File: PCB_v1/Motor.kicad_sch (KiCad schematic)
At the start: 18 parts, among them J10 B4B-XH-A, U6 DRV8834PWP

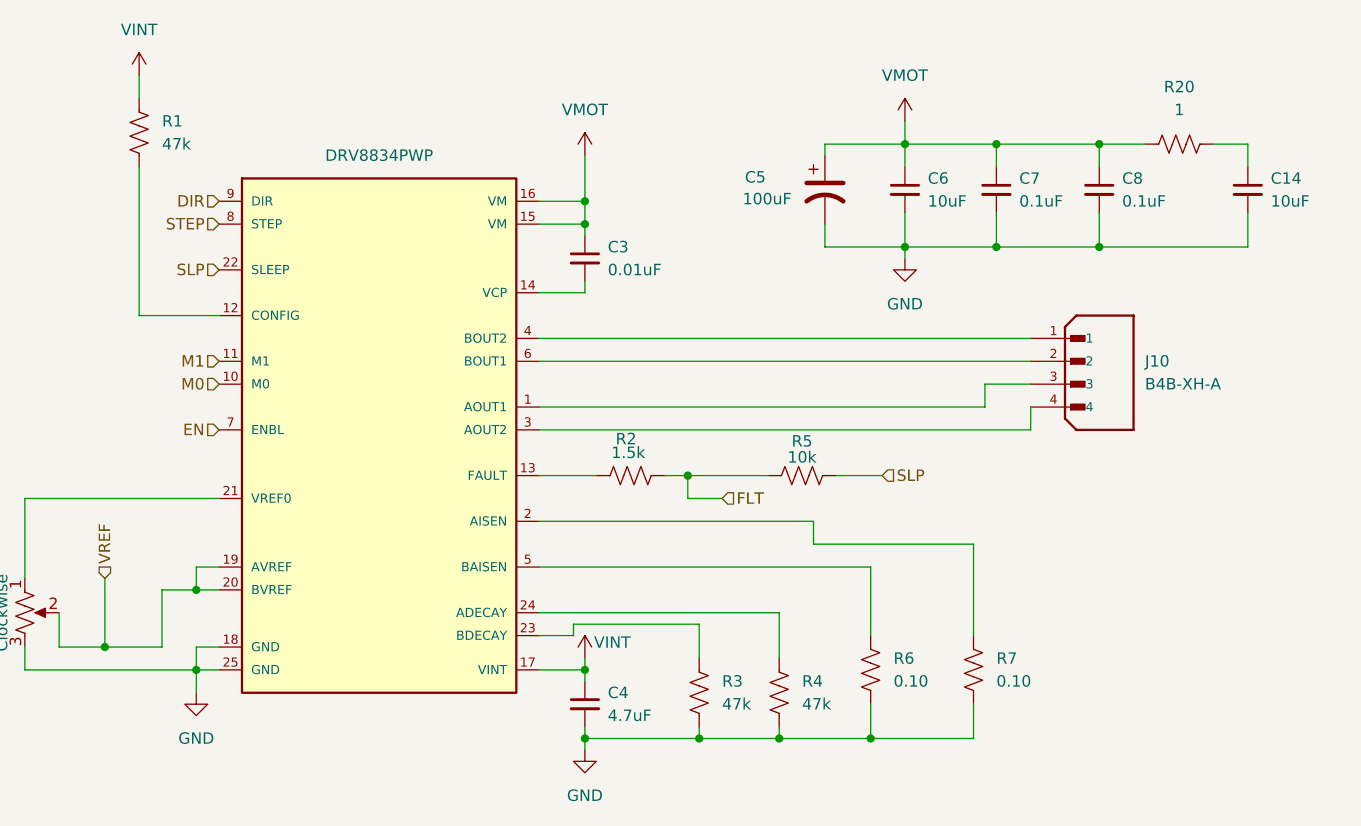
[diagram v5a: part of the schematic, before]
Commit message: Update before adding AGND for the power delivery
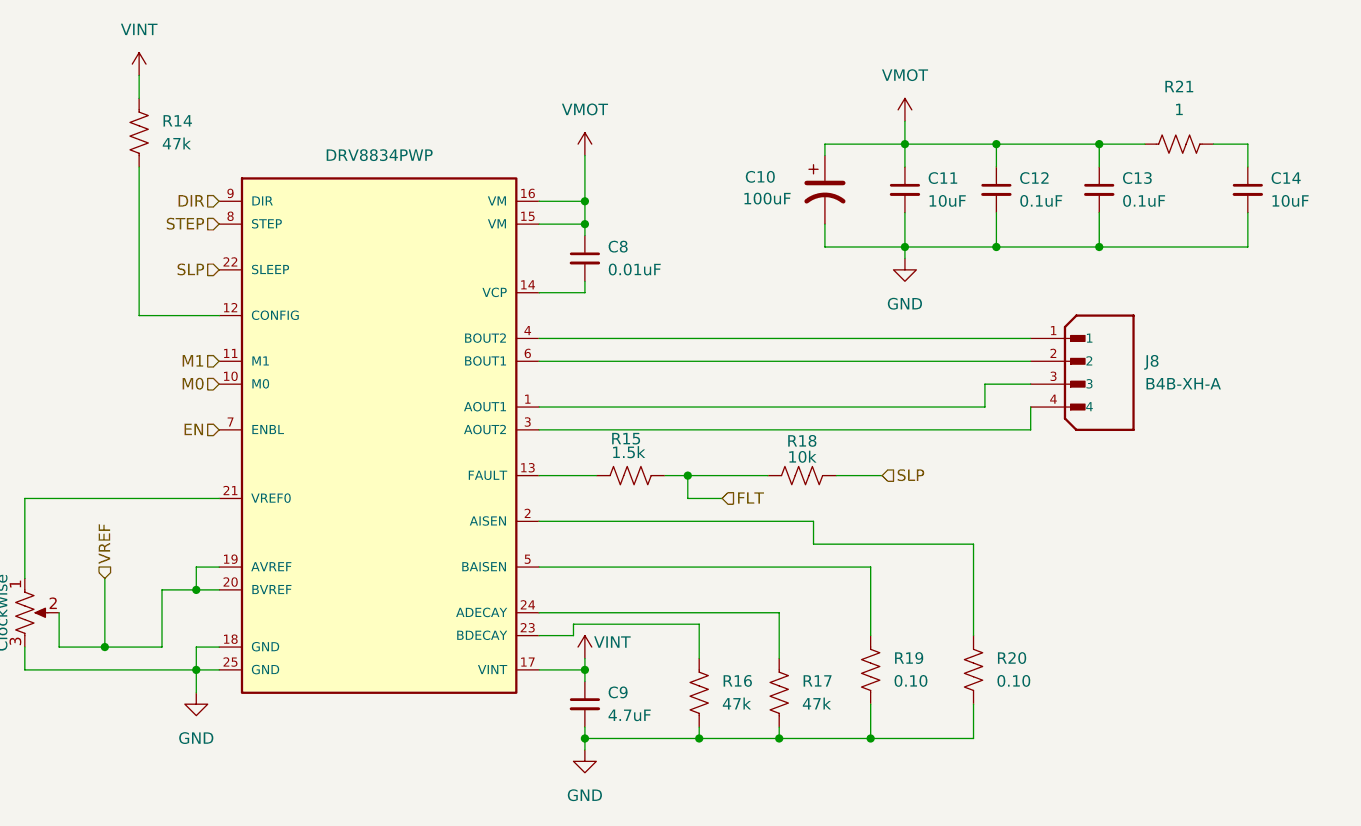
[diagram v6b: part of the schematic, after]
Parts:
- renumbered C5 to C10, C6 to C11, C7 to C12, C8 to C13, C3 to C8, C4 to C9, J10 to J8, R1 to R14, R2 to R15, R3 to R16, R4 to R17, R5 to R18, R6 to R19, R7 to R20, R20 to R21, U6 to U4
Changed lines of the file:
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@@
 		(dnp no)
 		(fields_autoplaced yes)
-		(property "Reference" "#PWR073"
+		(property "Reference" "#PWR074"
 			(at 256.54 96.52 0)
 			(effects
@@
 			(project "tuner time"
 				(path "/353cef6a-fb6e-40d9-89f8-eb54b7aa5118/2d8cfae4-f7d1-4a7d-b5cb-7588b4c1e8a5"
-					(reference "#PWR073")
+					(reference "#PWR074")
 					(unit 1)
 				)
@@
 		(dnp no)
 		(fields_autoplaced yes)
-		(property "Reference" "R1"
+		(property "Reference" "R14"
 			(at 81.28 57.1499 0)
 			(effects
@@
 			(project "tuner time"
 				(path "/353cef6a-fb6e-40d9-89f8-eb54b7aa5118/2d8cfae4-f7d1-4a7d-b5cb-7588b4c1e8a5"
-					(reference "R1")
+					(reference "R14")
 					(unit 1)
 				)
@@
 		(dnp no)
 		(fields_autoplaced yes)
-		(property "Reference" "#PWR070"
+		(property "Reference" "#PWR073"
 			(at 245.11 93.98 0)
 			(effects
@@
 			(project "tuner time"
 				(path "/353cef6a-fb6e-40d9-89f8-eb54b7aa5118/2d8cfae4-f7d1-4a7d-b5cb-7588b4c1e8a5"
-					(reference "#PWR070")
+					(reference "#PWR073")
 					(unit 1)
 				)
@@
 		(dnp no)
 		(fields_autoplaced yes)
-		(property "Reference" "R3"
+		(property "Reference" "R16"
 			(at 143.51 119.3799 0)
 			(effects
@@
 			(project "tuner time"
 				(path "/353cef6a-fb6e-40d9-89f8-eb54b7aa5118/2d8cfae4-f7d1-4a7d-b5cb-7588b4c1e8a5"
-					(reference "R3")
+					(reference "R16")
 					(unit 1)
 				)
@@
 		(dnp no)
 		(fields_autoplaced yes)
-		(property "Reference" "R20"
+		(property "Reference" "R21"
 			(at 194.31 53.34 90)
 			(effects
@@
 			(project "tuner time"
 				(path "/353cef6a-fb6e-40d9-89f8-eb54b7aa5118/2d8cfae4-f7d1-4a7d-b5cb-7588b4c1e8a5"
-					(reference "R20")
+					(reference "R21")
 					(unit 1)
 				)
@@
 		(dnp no)
 		(fields_autoplaced yes)
-		(property "Reference" "C3"
+		(property "Reference" "C8"
 			(at 130.81 71.1262 0)
 			(effects
@@
 			(project "tuner time"
 				(path "/353cef6a-fb6e-40d9-89f8-eb54b7aa5118/2d8cfae4-f7d1-4a7d-b5cb-7588b4c1e8a5"
-					(reference "C3")
+					(reference "C8")
 					(unit 1)
 				)
@@
 		(dnp no)
 		(fields_autoplaced yes)
-		(property "Reference" "#PWR067"
+		(property "Reference" "#PWR070"
 			(at 163.83 60.96 0)
 			(effects
@@
 			(project "tuner time"
 				(path "/353cef6a-fb6e-40d9-89f8-eb54b7aa5118/2d8cfae4-f7d1-4a7d-b5cb-7588b4c1e8a5"
-					(reference "#PWR067")
+					(reference "#PWR070")
 					(unit 1)
 				)
@@
 		(dnp no)
 		(fields_autoplaced yes)
-		(property "Reference" "#PWR064"
+		(property "Reference" "#PWR067"
 			(at 128.27 64.77 0)
 			(effects
@@
 			(project "tuner time"
 				(path "/353cef6a-fb6e-40d9-89f8-eb54b7aa5118/2d8cfae4-f7d1-4a7d-b5cb-7588b4c1e8a5"
-					(reference "#PWR064")
+					(reference "#PWR067")
 					(unit 1)
 				)
@@
 		(dnp no)
 		(fields_autoplaced yes)
-		(property "Reference" "#PWR066"
+		(property "Reference" "#PWR069"
 			(at 128.27 133.35 0)
 			(effects
@@
 			(project "tuner time"
 				(path "/353cef6a-fb6e-40d9-89f8-eb54b7aa5118/2d8cfae4-f7d1-4a7d-b5cb-7588b4c1e8a5"
-					(reference "#PWR066")
+					(reference "#PWR069")
 					(unit 1)
 				)
@@
 		(dnp no)
 		(fields_autoplaced yes)
-		(property "Reference" "#PWR063"
+		(property "Reference" "#PWR065"
 			(at 78.74 55.88 0)
 			(effects
@@
 			(project "tuner time"
 				(path "/353cef6a-fb6e-40d9-89f8-eb54b7aa5118/2d8cfae4-f7d1-4a7d-b5cb-7588b4c1e8a5"
-					(reference "#PWR063")
+					(reference "#PWR065")
 					(unit 1)
 				)
@@
 		(dnp no)
 		(fields_autoplaced yes)
-		(property "Reference" "#PWR062"
+		(property "Reference" "#PWR066"
 			(at 85.09 127 0)
 			(effects
@@
 			(project "tuner time"
 				(path "/353cef6a-fb6e-40d9-89f8-eb54b7aa5118/2d8cfae4-f7d1-4a7d-b5cb-7588b4c1e8a5"
-					(reference "#PWR062")
+					(reference "#PWR066")
 					(unit 1)
 				)
@@
 		(dnp no)
 		(fields_autoplaced yes)
-		(property "Reference" "R4"
+		(property "Reference" "R17"
 			(at 152.4 119.3799 0)
 			(effects
@@
 			(project "tuner time"
 				(path "/353cef6a-fb6e-40d9-89f8-eb54b7aa5118/2d8cfae4-f7d1-4a7d-b5cb-7588b4c1e8a5"
-					(reference "R4")
+					(reference "R17")
 					(unit 1)
 				)
@@
 		(dnp no)
 		(fields_autoplaced yes)
-		(property "Reference" "C7"
+		(property "Reference" "C12"
 			(at 176.53 63.5062 0)
 			(effects
@@
 			(project "tuner time"
 				(path "/353cef6a-fb6e-40d9-89f8-eb54b7aa5118/2d8cfae4-f7d1-4a7d-b5cb-7588b4c1e8a5"
-					(reference "C7")
+					(reference "C12")
 					(unit 1)
 				)
@@
 		(dnp no)
 		(fields_autoplaced yes)
-		(property "Reference" "U6"
+		(property "Reference" "U4"
 			(at 105.41 58.42 0)
 			(effects
@@
 			(project "tuner time"
 				(path "/353cef6a-fb6e-40d9-89f8-eb54b7aa5118/2d8cfae4-f7d1-4a7d-b5cb-7588b4c1e8a5"
-					(reference "U6")
+					(reference "U4")
 					(unit 1)
 				)
@@
 		(dnp no)
 		(fields_autoplaced yes)
-		(property "Reference" "#PWR069"
+		(property "Reference" "#PWR072"
 			(at 238.76 93.98 0)
 			(effects
@@
 			(project "tuner time"
 				(path "/353cef6a-fb6e-40d9-89f8-eb54b7aa5118/2d8cfae4-f7d1-4a7d-b5cb-7588b4c1e8a5"
-					(reference "#PWR069")
+					(reference "#PWR072")
 					(unit 1)
 				)
@@
 		(dnp no)
 		(fields_autoplaced yes)
-		(property "Reference" "C8"
+		(property "Reference" "C13"
 			(at 187.96 63.5062 0)
 			(effects
@@
 			(project "tuner time"
 				(path "/353cef6a-fb6e-40d9-89f8-eb54b7aa5118/2d8cfae4-f7d1-4a7d-b5cb-7588b4c1e8a5"
-					(reference "C8")
+					(reference "C13")
 					(unit 1)
 				)
@@
 		(dnp no)
 		(fields_autoplaced yes)
-		(property "Reference" "#PWR068"
+		(property "Reference" "#PWR071"
 			(at 163.83 78.74 0)
 			(effects
@@
 			(project "tuner time"
 				(path "/353cef6a-fb6e-40d9-89f8-eb54b7aa5118/2d8cfae4-f7d1-4a7d-b5cb-7588b4c1e8a5"
-					(reference "#PWR068")
+					(reference "#PWR071")
 					(unit 1)
 				)
@@
 		(dnp no)
 		(fields_autoplaced yes)
-		(property "Reference" "C6"
+		(property "Reference" "C11"
 			(at 166.37 63.5062 0)
 			(effects
@@
 			(project "tuner time"
 				(path "/353cef6a-fb6e-40d9-89f8-eb54b7aa5118/2d8cfae4-f7d1-4a7d-b5cb-7588b4c1e8a5"
-					(reference "C6")
+					(reference "C11")
 					(unit 1)
 				)
@@
 		(on_board yes)
 		(dnp no)
-		(property "Reference" "#PWR061"
+		(property "Reference" "#PWR068"
 			(at 128.27 120.65 0)
 			(effects
@@
 			(project "tuner time"
 				(path "/353cef6a-fb6e-40d9-89f8-eb54b7aa5118/2d8cfae4-f7d1-4a7d-b5cb-7588b4c1e8a5"
-					(reference "#PWR061")
+					(reference "#PWR068")
 					(unit 1)
 				)
@@
 		(dnp no)
 		(fields_autoplaced yes)
-		(property "Reference" "R6"
+		(property "Reference" "R19"
 			(at 162.56 116.8399 0)
 			(effects
@@
 			(project "tuner time"
 				(path "/353cef6a-fb6e-40d9-89f8-eb54b7aa5118/2d8cfae4-f7d1-4a7d-b5cb-7588b4c1e8a5"
-					(reference "R6")
+					(reference "R19")
 					(unit 1)
 				)
@@
 		(dnp no)
 		(fields_autoplaced yes)
-		(property "Reference" "J10"
+		(property "Reference" "J8"
 			(at 190.5 83.8199 0)
 			(effects
@@
 			(project ""
 				(path "/353cef6a-fb6e-40d9-89f8-eb54b7aa5118/2d8cfae4-f7d1-4a7d-b5cb-7588b4c1e8a5"
-					(reference "J10")
+					(reference "J8")
 					(unit 1)
 				)
@@
 		(dnp no)
 		(fields_autoplaced yes)
-		(property "Reference" "C4"
+		(property "Reference" "C9"
 			(at 130.81 120.6562 0)
 			(effects
@@
 			(project "tuner time"
 				(path "/353cef6a-fb6e-40d9-89f8-eb54b7aa5118/2d8cfae4-f7d1-4a7d-b5cb-7588b4c1e8a5"
-					(reference "C4")
+					(reference "C9")
 					(unit 1)
 				)
@@
 		(on_board yes)
 		(dnp no)
-		(property "Reference" "R2"
+		(property "Reference" "R15"
 			(at 132.842 92.456 90)
 			(effects
@@
 			(project "tuner time"
 				(path "/353cef6a-fb6e-40d9-89f8-eb54b7aa5118/2d8cfae4-f7d1-4a7d-b5cb-7588b4c1e8a5"
-					(reference "R2")
+					(reference "R15")
 					(unit 1)
 				)
@@
 		(on_board yes)
 		(dnp no)
-		(property "Reference" "C5"
+		(property "Reference" "C10"
 			(at 146.05 63.3729 0)
 			(effects
@@
 			(project "tuner time"
 				(path "/353cef6a-fb6e-40d9-89f8-eb54b7aa5118/2d8cfae4-f7d1-4a7d-b5cb-7588b4c1e8a5"
-					(reference "C5")
+					(reference "C10")
 					(unit 1)
 				)
@@
 		(on_board yes)
 		(dnp no)
-		(property "Reference" "R5"
+		(property "Reference" "R18"
 			(at 152.4 92.71 90)
 			(effects
@@
 			(project "tuner time"
 				(path "/353cef6a-fb6e-40d9-89f8-eb54b7aa5118/2d8cfae4-f7d1-4a7d-b5cb-7588b4c1e8a5"
-					(reference "R5")
+					(reference "R18")
 					(unit 1)
 				)
@@
 		(dnp no)
 		(fields_autoplaced yes)
-		(property "Reference" "R7"
+		(property "Reference" "R20"
 			(at 173.99 116.8399 0)
 			(effects
@@
 			(project "tuner time"
 				(path "/353cef6a-fb6e-40d9-89f8-eb54b7aa5118/2d8cfae4-f7d1-4a7d-b5cb-7588b4c1e8a5"
-					(reference "R7")
-					(unit 1)
-				)
+					(reference "R20")
+					(unit 1)
+				)

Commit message: Initial placement draft
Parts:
- C10: footprint CAP_PAN_EEE_H13_PAN -> CAP_EEE1AA101WR
- J8: footprint B4B-XH-A:JST_B4B-XH-A -> Parts_Library:JST_B4B-XH-A
- RV1: value Clockwise -> 10k; footprint (none) -> Parts_Library:TRIM_TC33X-2-103E; MFP (none) -> TRIM_TC33X-2-103E
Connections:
- net A1: now reaches U4.1 (AOUT1)
- net A1: now also J8.4; no longer J8.3
- net A2: now reaches U4.3 (AOUT2)
- net A2: now also J8.3; no longer J8.4
- net B1: now reaches J8.1
- net B1: now also U4.6 (BOUT1); no longer U4.4 (BOUT2)
- net B2: now reaches J8.2
- net B2: now also U4.4 (BOUT2); no longer U4.6 (BOUT1)

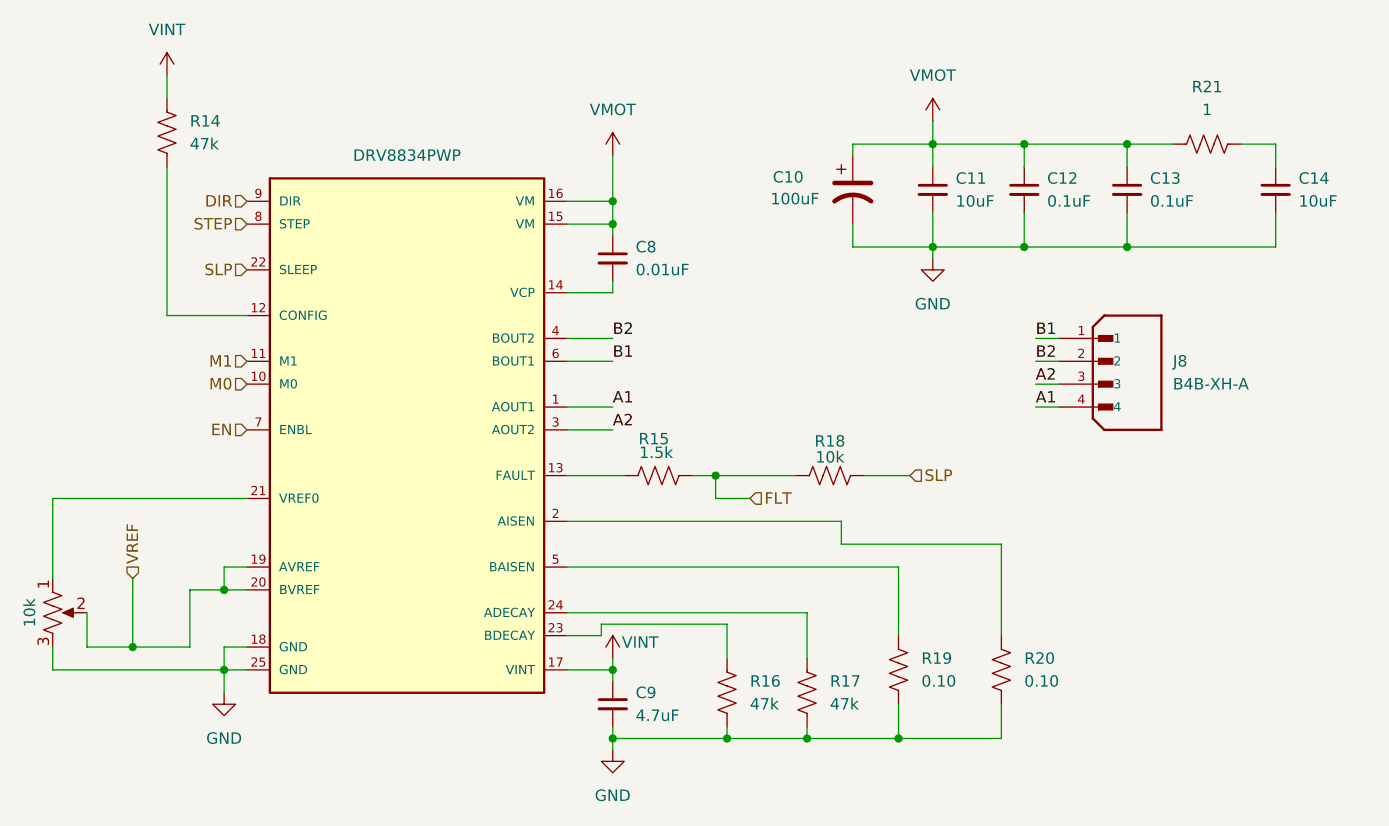
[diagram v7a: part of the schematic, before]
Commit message: adjusted placments
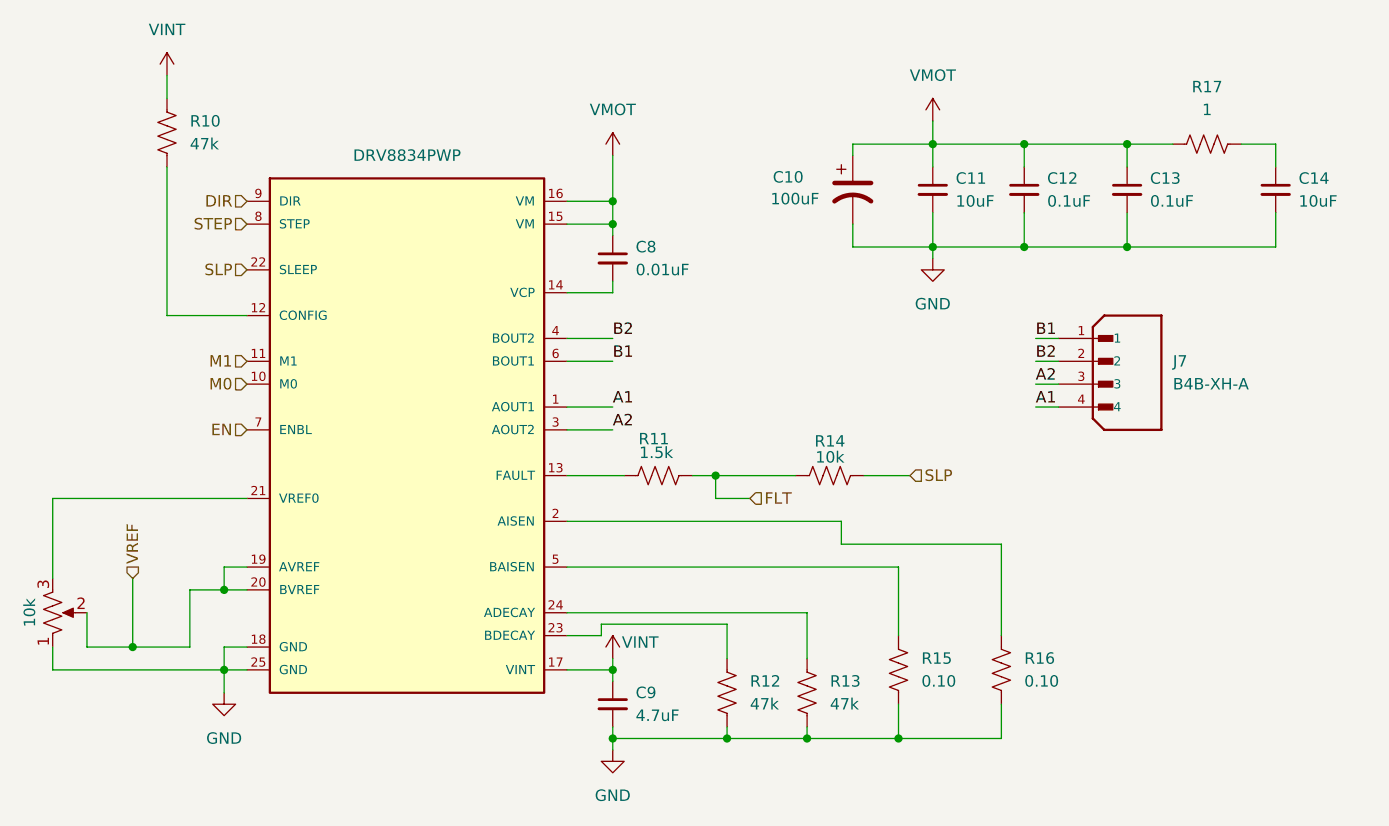
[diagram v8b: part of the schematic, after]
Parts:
- renumbered J8 to J7, R14 to R10, R15 to R11, R16 to R12, R17 to R13, R18 to R14, R19 to R15, R20 to R16, R21 to R17
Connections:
- net GND: now also RV1.1; no longer RV1.3
- net at U4.21 (VREF0): now also RV1.3; no longer RV1.1
